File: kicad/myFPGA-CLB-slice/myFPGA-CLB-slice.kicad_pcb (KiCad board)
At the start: 2 copper layers, 100 x 140 mm, 162 parts, among them J1 Conn_01x04, J10 Conn_01x02, J11 Conn_01x02, J12 Conn_01x04, J13 Conn_01x04, J14 Conn_01x04, J15 Conn_01x04, J16 Conn_01x02, J2 Conn_01x04, J3 Conn_01x04, J4 Conn_01x04, J5 Conn_01x04, J6 Conn_01x04, J7 Conn_01x04, J8 Conn_01x02, J9 Conn_01x04, U1 NC7SB3157P6X, U10 NC7SB3157P6X, U11 NC7SB3157P6X, U12 NC7SB3157P6X, U13 74LS157, U14 NC7SB3157P6X, U15 NC7SB3157P6X, U16 NC7SB3157P6X, U17 NC7SB3157P6X, U18 74LS175, U19 74AHCT595, U2 74AHCT595, U20 74AHCT595, U21 74LS151, U22 74LS151, U23 NC7SB3157P6X, U24 74AHCT595, U25 74AHCT595, U26 74LS151, U27 74LS151, U28 NC7SB3157P6X, U29 74AHCT595, U3 74AHCT595, U30 74AHCT595, U31 74LS151, U32 74LS151, U33 NC7SB3157P6X, U34 74LS153, U35 74LS153, U36 74LS153, U37 74LS153, U38 74AHCT595, U39 NC7SB3157P6X, U4 74AHCT595, U40 NC7SB3157P6X, U5 74LS151, U6 74LS151, U7 NC7SB3157P6X, U8 74HC86, U9 NC7SB3157P6X

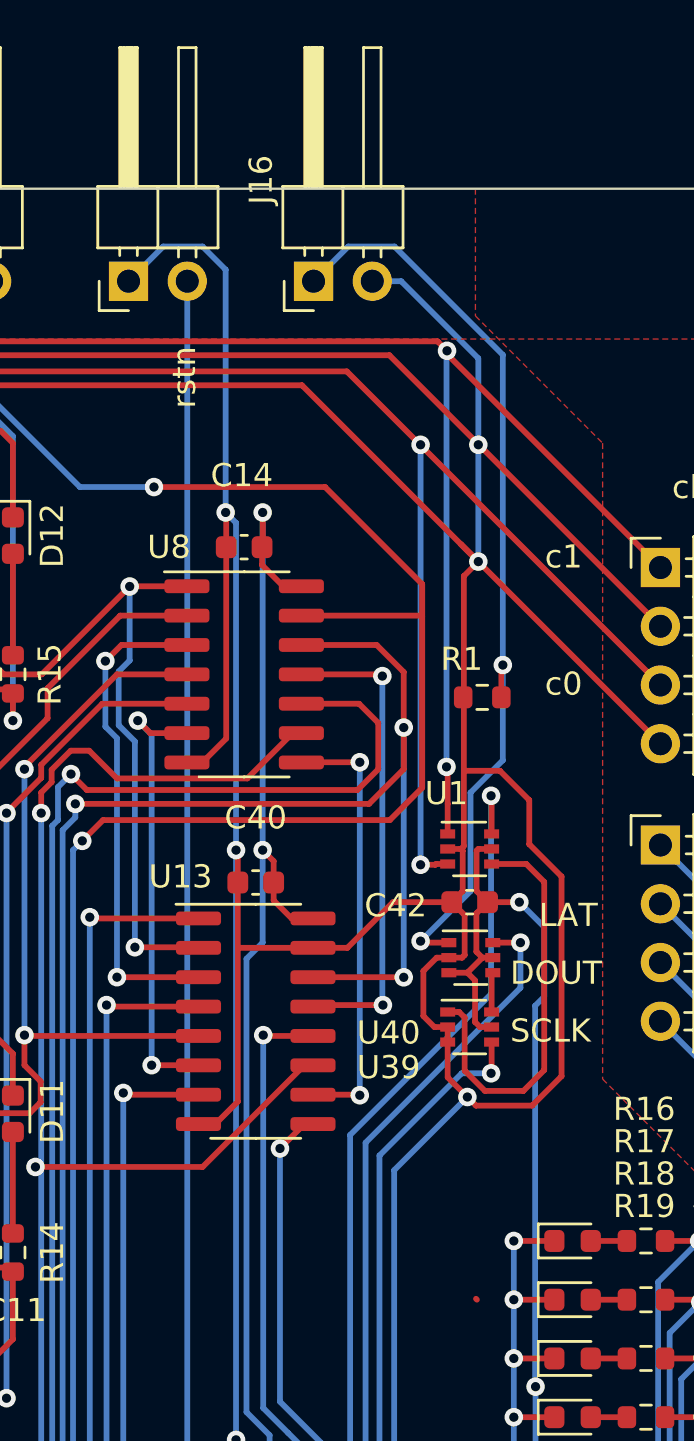
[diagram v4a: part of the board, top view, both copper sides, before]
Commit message: found more bugs
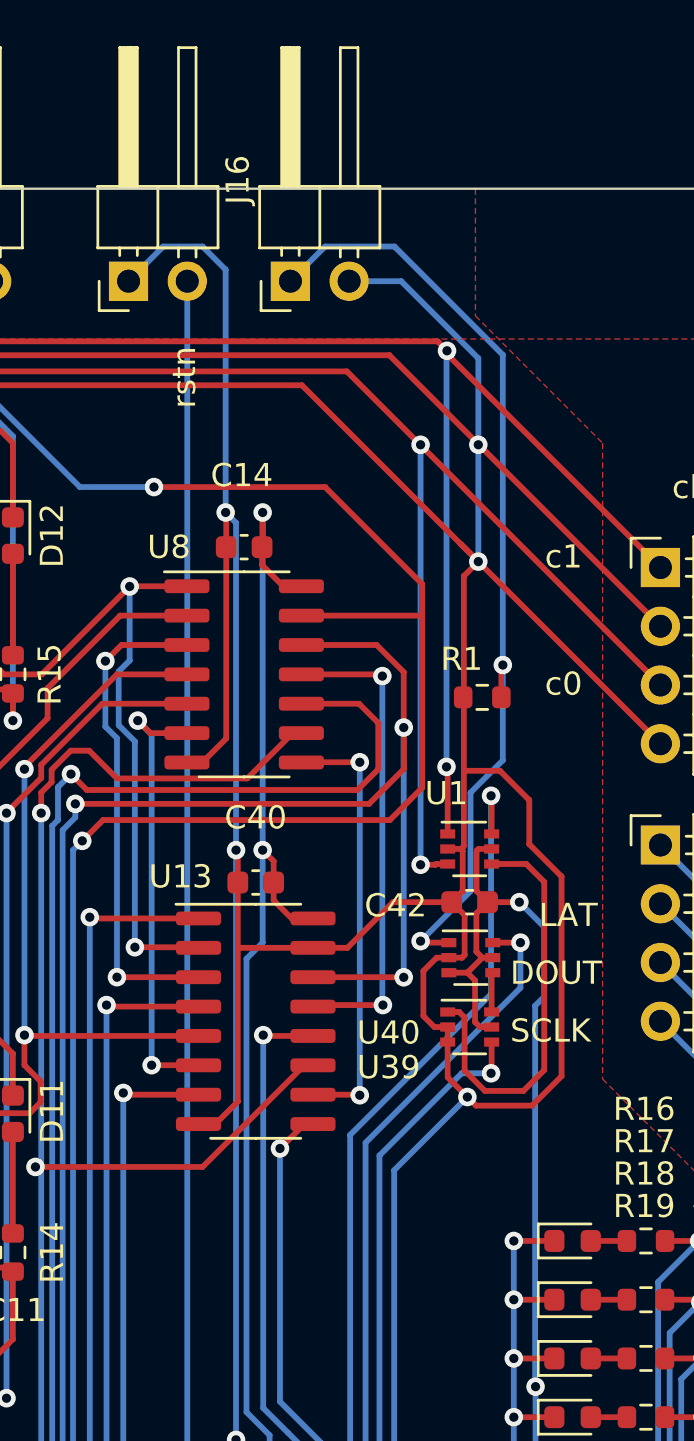
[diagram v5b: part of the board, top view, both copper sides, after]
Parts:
- moved J16 1.00 mm to (124.0, 34.0)
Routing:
- net /ext_ce: track 40.2 -> 41.2 mm
- net GND: track 1712.3 -> 1713.3 mm
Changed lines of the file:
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@@
       (disableapertmacros false)
       (usegerberextensions true)
-      (usegerberattributes false)
+      (usegerberattributes true)
       (usegerberadvancedattributes false)
       (creategerberjobfile false)
@@
       (drillshape 0)
       (scaleselection 1)
-      (outputdirectory "plots")
+      (outputdirectory "plots-r2")
     )
   )
@@
   )
   (footprint "Connector_PinHeader_2.54mm:PinHeader_1x02_P2.54mm_Horizontal" locked (layer "F.Cu")
-    (at 125 34 90)
+    (at 124 34 90)
     (descr "Through hole angled pin header, 1x02, 2.54mm pitch, 6mm pin length, single row")
     (tags "Through hole angled pin header THT 1x02 2.54mm single row")
@@
   (segment (start 99.8 60.3) (end 99.775 60.275) (width 0.25) (layer "F.Cu") (net 2))
   (segment (start 57.075 51.925) (end 57.075 42.725) (width 0.25) (layer "F.Cu") (net 2))
-  (segment (start 132.065 78.04) (end 132.025 78) (width 0.25) (layer "F.Cu") (net 2))
   (segment (start 69.5 106.225) (end 69.5 105.5) (width 0.25) (layer "F.Cu") (net 2))
   (segment (start 63.9375 76.213) (end 63.7245 76) (width 0.25) (layer "F.Cu") (net 2))
@@
   (segment (start 63.5755 90.9) (end 63.5755 106) (width 0.25) (layer "B.Cu") (net 2))
   (segment (start 132.1 100) (end 132.1 104.6) (width 0.25) (layer "B.Cu") (net 2))
+  (segment (start 132.125 37.335695) (end 132.125 46.125) (width 0.25) (layer "B.Cu") (net 2))
   (segment (start 108.5 129.75) (end 108.5 144.9) (width 0.25) (layer "B.Cu") (net 2))
   (segment (start 94.5 80.6) (end 94.5 105.6) (width 0.25) (layer "B.Cu") (net 2))
@@
   (segment (start 132.1 104.6) (end 132.1 140.7) (width 0.25) (layer "B.Cu") (net 2))
   (segment (start 88.5 84) (end 88.5 93.75) (width 0.25) (layer "B.Cu") (net 2))
-  (segment (start 127.54 34) (end 128.789305 34) (width 0.25) (layer "B.Cu") (net 2))
   (segment (start 88.5 80.8) (end 88.5 84) (width 0.25) (layer "B.Cu") (net 2))
   (segment (start 128.994 103.81) (end 128.105 104.699) (width 0.25) (layer "B.Cu") (net 2))
@@
   (segment (start 140 58.38) (end 146.225 64.605) (width 0.25) (layer "B.Cu") (net 2))
   (segment (start 146.225 137.235) (end 140 143.46) (width 0.25) (layer "B.Cu") (net 2))
+  (segment (start 128.789305 34) (end 132.125 37.335695) (width 0.25) (layer "B.Cu") (net 2))
   (segment (start 62.8 133.3) (end 63.5755 132.5245) (width 0.25) (layer "B.Cu") (net 2))
   (segment (start 122.9 117.8) (end 123 117.7) (width 0.25) (layer "B.Cu") (net 2))
@@
   (segment (start 63.6 75.9755) (end 63.5755 76) (width 0.25) (layer "B.Cu") (net 2))
   (segment (start 123 125.6) (end 125.8 128.4) (width 0.25) (layer "B.Cu") (net 2))
-  (segment (start 128.789305 34) (end 132.125 37.335695) (width 0.25) (layer "B.Cu") (net 2))
   (segment (start 88.5 105.75) (end 88.5 118.75) (width 0.25) (layer "B.Cu") (net 2))
   (segment (start 123 90.6) (end 123 117.7) (width 0.25) (layer "B.Cu") (net 2))
-  (segment (start 132.125 37.335695) (end 132.125 46.125) (width 0.25) (layer "B.Cu") (net 2))
   (segment (start 108.5 41.2) (end 108.5 66.25) (width 0.25) (layer "B.Cu") (net 2))
   (segment (start 88.5 139.7) (end 88.5 144.8) (width 0.25) (layer "B.Cu") (net 2))
+  (segment (start 126.54 34) (end 128.789305 34) (width 0.25) (layer "B.Cu") (net 2))
   (segment (start 99.8 49.2755) (end 99.8 144.8) (width 0.25) (layer "B.Cu") (net 2))
   (segment (start 121.6495 89.2495) (end 123 90.6) (width 0.25) (layer "B.Cu") (net 2))
@@
   (via (at 133.185 50.597) (size 0.8) (drill 0.4) (layers "F.Cu" "B.Cu") (net 192))
   (via (at 129.629 62.535) (size 0.8) (drill 0.4) (layers "F.Cu" "B.Cu") (net 192))
+  (segment (start 128.5 32.5) (end 125.5 32.5) (width 0.25) (layer "B.Cu") (net 192))
   (segment (start 129.629 62.535) (end 131.788 60.376) (width 0.25) (layer "B.Cu") (net 192))
-  (segment (start 128.5 32.5) (end 126.5 32.5) (width 0.25) (layer "B.Cu") (net 192))
   (segment (start 133.185 50.597) (end 133.185 37.185) (width 0.25) (layer "B.Cu") (net 192))
   (segment (start 131.788 56.113695) (end 133.185 54.716695) (width 0.25) (layer "B.Cu") (net 192))
+  (segment (start 125.5 32.5) (end 124 34) (width 0.25) (layer "B.Cu") (net 192))
   (segment (start 131.788 60.376) (end 131.788 56.113695) (width 0.25) (layer "B.Cu") (net 192))
-  (segment (start 126.5 32.5) (end 125 34) (width 0.25) (layer "B.Cu") (net 192))
-  (segment (start 133.185 37.185) (end 128.5 32.5) (width 0.25) (layer "B.Cu") (net 192))
   (segment (start 133.185 54.716695) (end 133.185 50.597) (width 0.25) (layer "B.Cu") (net 192))
+  (segment (start 133.185 37.185) (end 128.5 32.5) (width 0.25) (layer "B.Cu") (net 192))
   (segment (start 127.475 119.095) (end 129.5 119.095) (width 0.25) (layer "F.Cu") (net 193))
   (segment (start 137.58 119.095) (end 129.5 119.095) (width 0.25) (layer "F.Cu") (net 193))
